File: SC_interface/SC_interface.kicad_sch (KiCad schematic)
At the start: 24 parts, among them J101 5V_PWR, J102 J_chassis, SW101 Main Power, SW102 Master SW, U101 JCA0305D03

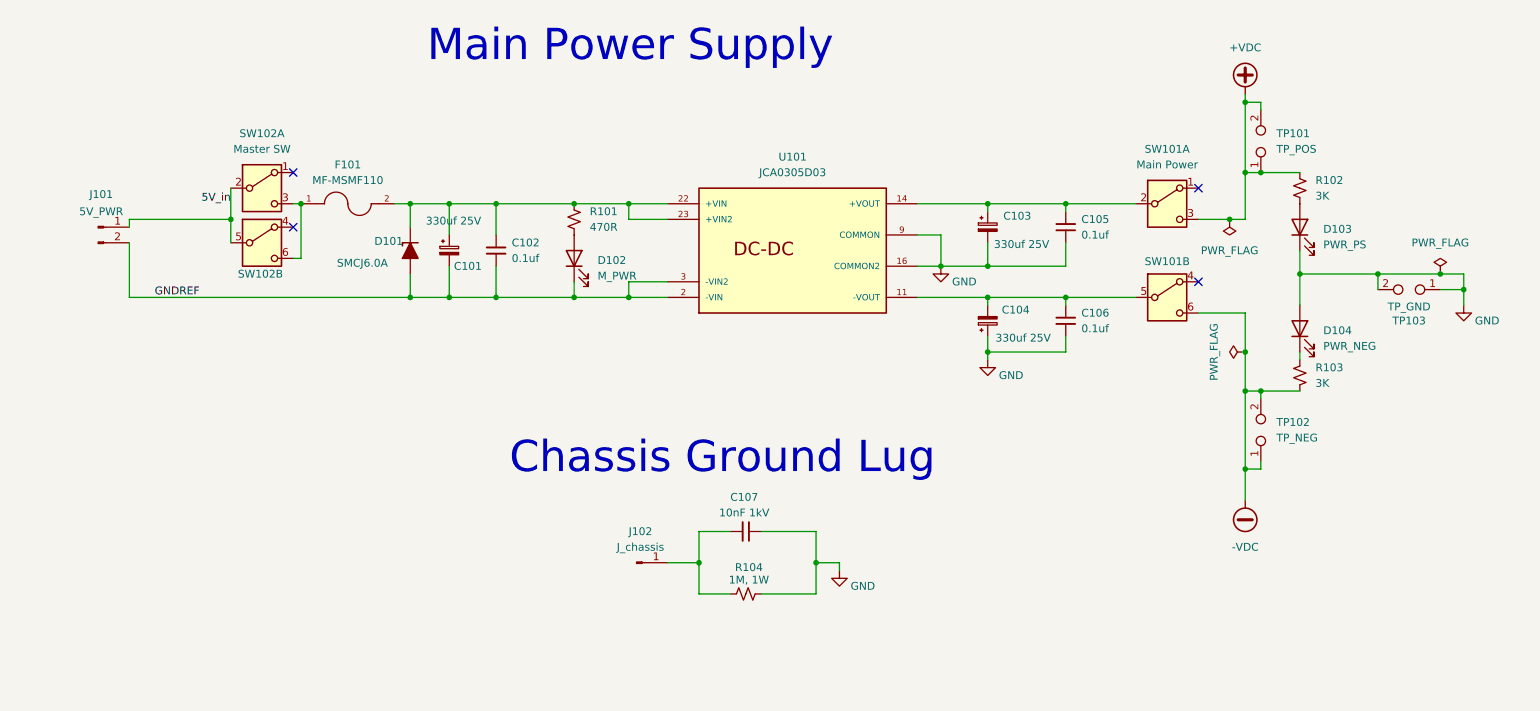
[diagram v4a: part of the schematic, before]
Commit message: schematic changes
1. added TVS at output of DC-DC convert to prevent kick back
2. Changed all diodes to BAV199
3. change the Cfeedback to 4.7uF
4. removed LND Fet, replaced it with 4.7 K ohm
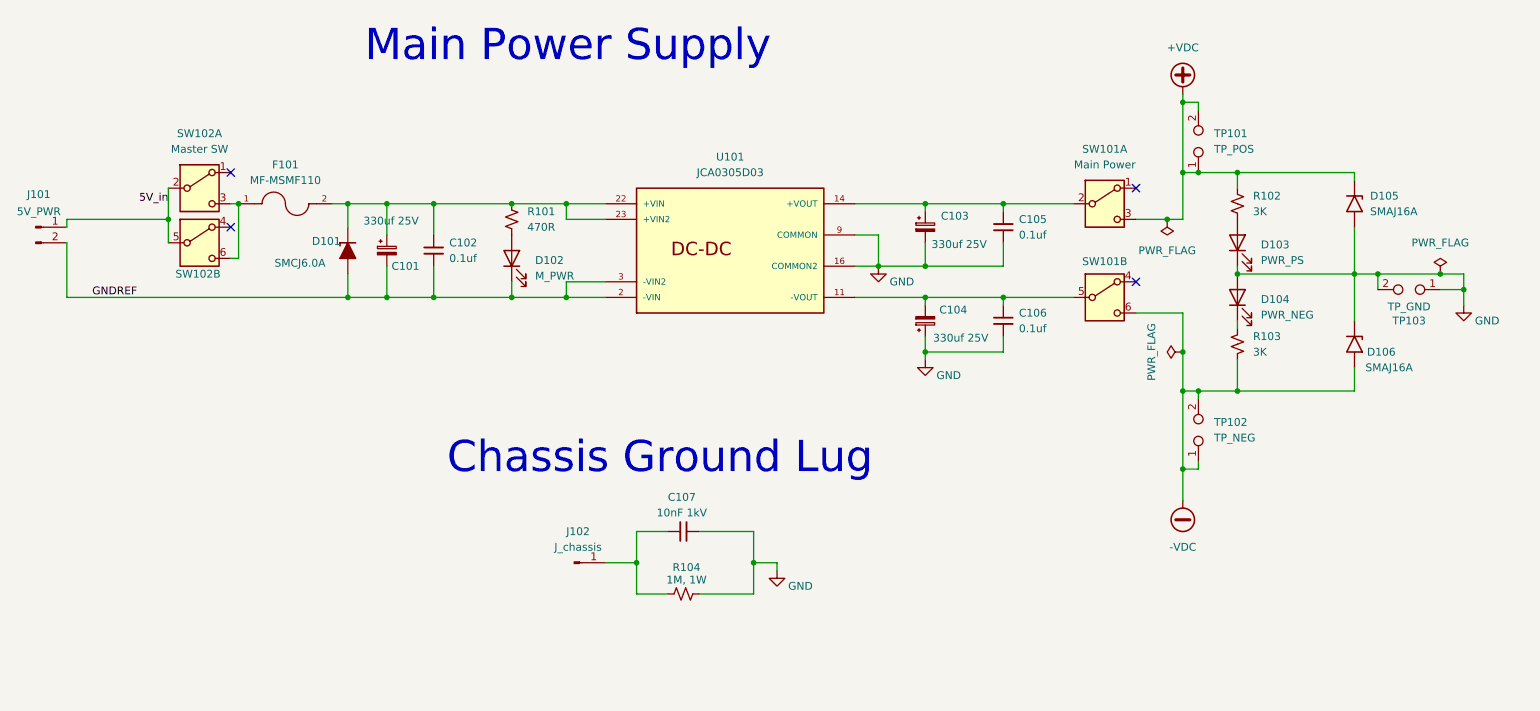
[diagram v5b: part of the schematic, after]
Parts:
- added D105, D106: SMAJ16A, Diode_SMD:D_SMA, symbol Diode:SMAJ16A
- D102, D103, D104: footprint PCM_SparkFun-Resistor:R_0603_1608Metric -> Connector_PinHeader_2.54mm:PinHeader_1x02_P2.54mm_Vertical
- R101, R102, R103: footprint PCM_SparkFun-Resistor:R_0603_1608Metric -> Resistor_SMD:R_0805_2012Metric_Pad1.20x1.40mm_HandSolder
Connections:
- net +VDC: now also D105.1 (A1)
- net -VDC: now also D106.2 (A2)
- net GND: now also D105.2 (A2), D106.1 (A1)
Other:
- moved on the sheet: C101, C102, C103, C104, C105, C106, C107, D101, D102, D103, D104, F101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
